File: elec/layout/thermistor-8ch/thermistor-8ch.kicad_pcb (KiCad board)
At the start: 4 copper layers, 29.7 x 28.3 mm, 78 parts, among them U5 10µH ±20%

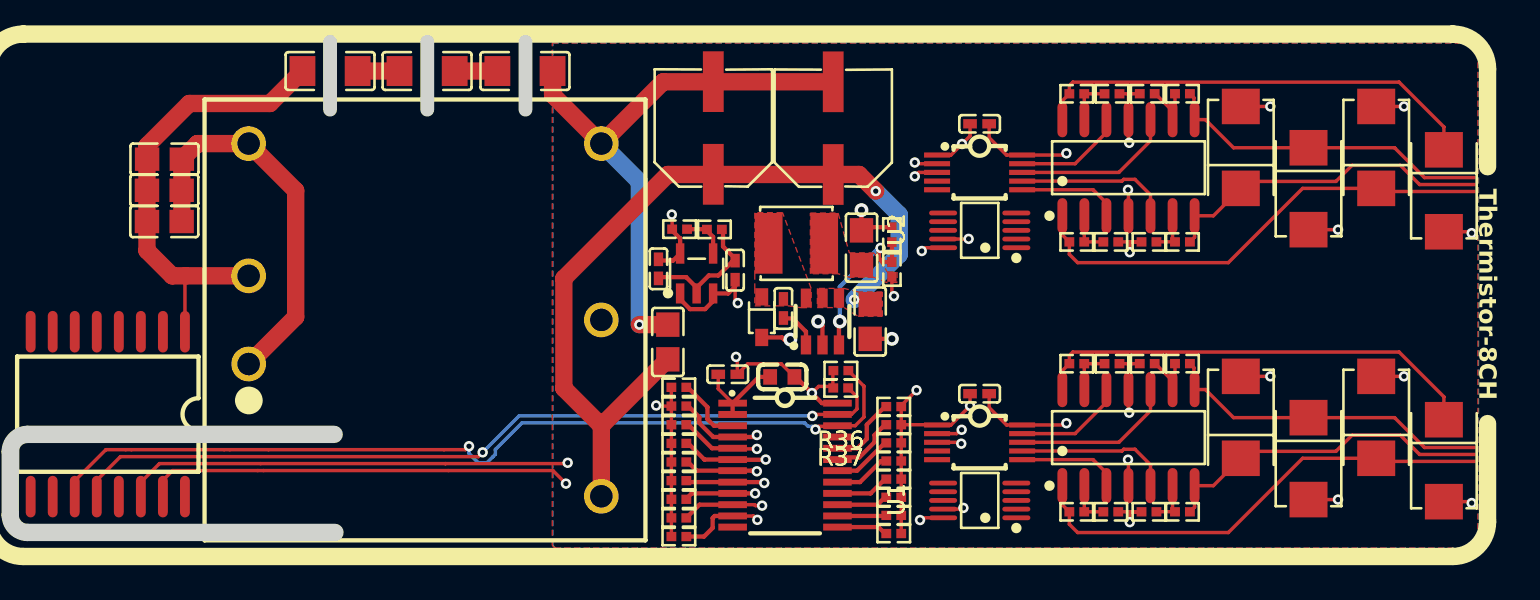
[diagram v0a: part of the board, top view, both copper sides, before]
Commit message: connect up ADC to thermistor outputs
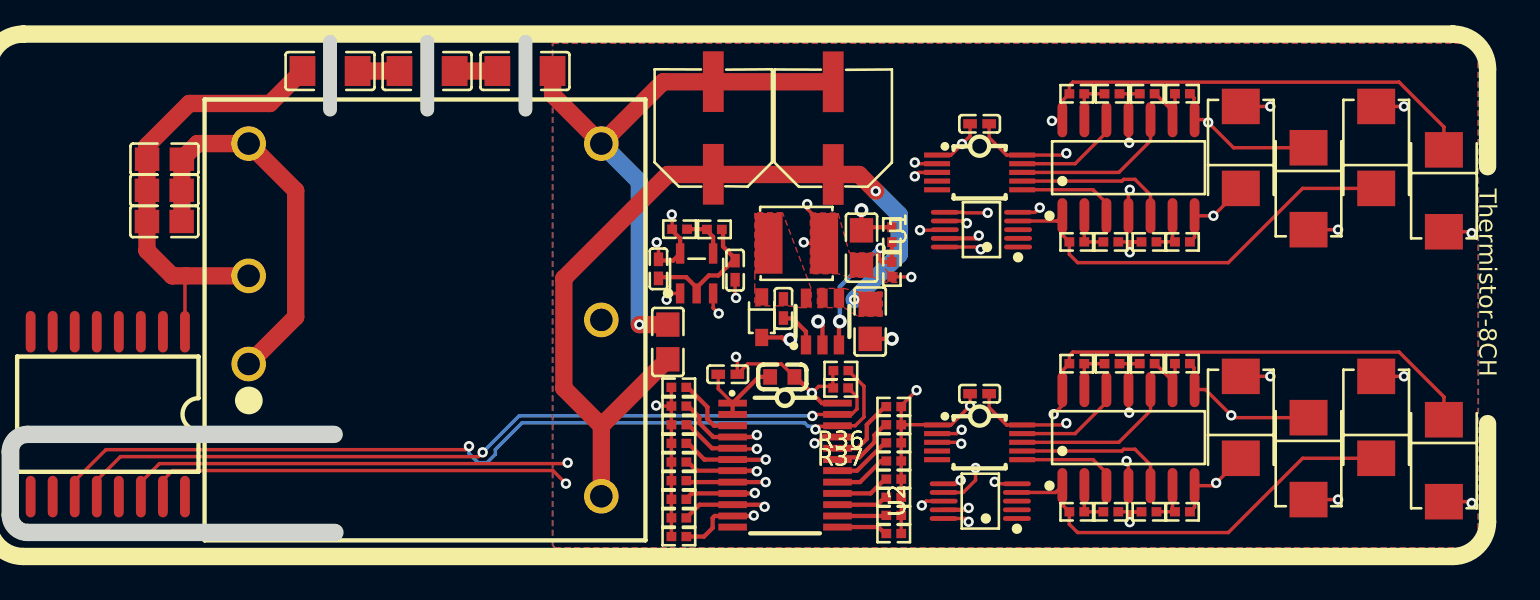
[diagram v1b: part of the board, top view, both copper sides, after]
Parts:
- moved U1 15.6 mm to (109.6, 88.7)
- moved U2 15.6 mm to (109.6, 104.3)
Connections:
- net SW renamed cathode
- net dac_1_4-IN3plus renamed IN3plus
- net dac_1_4-VOUTD renamed dac_1_4-IN4plus
- net dac_5_8-IN3plus renamed VOUTC
- net dac_5_8-VOUTD renamed dac_5_8-IN4plus
- C10 pad 1: hv-2 -> hv
- C10 pad 2: gnd -> gnd-1
- C11 pad 1: hv-2 -> hv
- C11 pad 2: gnd -> gnd-1
- C12 pad 1: hv-2 -> hv
- C12 pad 2: gnd -> gnd-1
- C13 pad 2: gnd-1 -> gnd
- C14 pad 2: gnd-1 -> gnd
- C15 pad 2: gnd-1 -> gnd
- C16 pad 1: gnd -> gnd-1
- C16 pad 2: regulator_24v_isolated-net -> regulator_24v_isolated-net-1
- C17 pad 1: regulator_24v_isolated-net -> regulator_24v_isolated-net-1
- C17 pad 2: regulator_24v_isolated-net-1 -> regulator_24v_isolated-net
- C18 pad 1: regulator_24v_isolated-net-1 -> regulator_24v_isolated-net
- C18 pad 2: gnd-1 -> gnd
- C2 pad 2: gnd-1 -> gnd
- C3 pad 1: hv -> hv-2
- C3 pad 2: gnd-1 -> gnd
- C4 pad 2: gnd-1 -> gnd
- C5 pad 2: gnd-1 -> gnd
- C6 pad 2: gnd-1 -> gnd
- C7 pad 2: gnd-1 -> gnd
- C8 pad 1: hv -> hv-2
- C8 pad 2: gnd-1 -> gnd
- C9 pad 2: gnd-1 -> gnd
- D1 pad 1: line-4 -> line-13
- D1 pad 2: gnd-1 -> gnd
- D2 pad 1: line-19 -> line-4
- D2 pad 2: gnd-1 -> gnd
- D3 pad 1: line-5 -> line-2
- D3 pad 2: gnd-1 -> gnd
- D4 pad 1: line-15 -> line-7
- D4 pad 2: gnd-1 -> gnd
- D5 pad 1: line-11 -> line-18
- D5 pad 2: gnd-1 -> gnd
- D6 pad 1: line-8 -> line-3
- D6 pad 2: gnd-1 -> gnd
- D7 pad 1: line-3 -> line-11
- D7 pad 2: gnd-1 -> gnd
- D8 pad 1: line-13 -> line
- D8 pad 2: gnd-1 -> gnd
- R1 pad 2: gnd-1 -> gnd
- R10 pad 1: gnd-1 -> gnd
- R11 pad 2: line-11 -> line-18
- R12 pad 1: gnd-1 -> gnd
- R13 pad 2: line-8 -> line-3
- R14 pad 1: gnd-1 -> gnd
- R15 pad 2: line-3 -> line-11
- R16 pad 1: gnd-1 -> gnd
- R17 pad 2: line-13 -> line
- R18 pad 1: gnd-1 -> gnd
- R19 pad 1: line-10 -> line-12
- R2 pad 1: hv -> hv-2
- R20 pad 1: line-18 -> line-10
- R21 pad 1: line-1 -> line-5
- R22 pad 1: line-12 -> line-16
- R23 pad 1: line-9 -> line-6
- R24 pad 1: line -> line-14
- R25 pad 1: line-7 -> line-8
- R26 pad 1: line-14 -> line-19
- R3 pad 2: line-4 -> line-13
- R36 pad 1: line-2 -> line-17
- R37 pad 1: line-6 -> line-9
- R38 pad 2: gnd-1 -> gnd
- R4 pad 1: gnd-1 -> gnd
- R5 pad 2: line-19 -> line-4
- R6 pad 1: gnd-1 -> gnd
- R7 pad 2: line-5 -> line-2
- R8 pad 1: gnd-1 -> gnd
- R9 pad 2: line-15 -> line-7
- U1 pad 1: gnd-1 -> gnd
- U1 pad 10: line-9 -> line-8
- U1 pad 2: adc_1_4-line-3 -> adc_1_4-line
- U1 pad 3: gnd-1 -> gnd
- U1 pad 4: adc_1_4-line-4 -> line-13
- U1 pad 5: adc_1_4-line-2 -> line-4
- U1 pad 6: adc_1_4-line -> line-2
- U1 pad 7: adc_1_4-line-1 -> line-7
- U1 pad 8: hv-4 -> hv-2
- U1 pad 9: line -> line-19
- U10 pad 1: gnd -> gnd-1
- U10 pad 11: line-2 -> line-17
- U10 pad 12: line-6 -> line-9
- U10 pad 15: gnd-1 -> gnd
- U10 pad 5: line-16 -> line-1
- U10 pad 6: line-17 -> line-15
- U11 pad 1: gnd-1 -> gnd
- U11 pad 10: line-14 -> line-19
- U11 pad 11: line-7 -> line-8
- U11 pad 12: gnd-1 -> gnd
- U11 pad 2: gnd-1 -> gnd
- U11 pad 21: gnd-1 -> gnd
- U11 pad 22: line-2 -> line-17
- U11 pad 23: line-6 -> line-9
- U11 pad 4: line-18 -> line-10
- U11 pad 5: line-10 -> line-12
- U11 pad 6: line-12 -> line-16
- U11 pad 7: line-1 -> line-5
- U11 pad 8: line -> line-14
- U11 pad 9: line-9 -> line-6
- U12 pad 1: hv -> hv-2
- U12 pad 2: gnd-1 -> gnd
- U12 pad 3: hv -> hv-2
- U13 pad 1: hv-2 -> hv
- U13 pad 2: gnd -> gnd-1
- U13 pad 3: hv-2 -> hv
- U13 pad 4: gnd-1 -> gnd
- U2 pad 1: gnd-1 -> gnd
- U2 pad 10: line-7 -> line-6
- U2 pad 2: adc_5_8-line-3 -> adc_5_8-line
- U2 pad 3: gnd-1 -> gnd
- U2 pad 4: adc_5_8-line -> line-18
- U2 pad 5: adc_5_8-line-1 -> line-3
- U2 pad 6: adc_5_8-line-4 -> line-11
- U2 pad 7: adc_5_8-line-2 -> line
- U2 pad 8: hv-4 -> hv-2
- U3 pad 2: gnd-1 -> gnd
- U4 pad 2: gnd-1 -> gnd
- U5 pad 2: hv -> hv-2
- U6 pad 1: line-4 -> line-13
- U6 pad 11: gnd-1 -> gnd
- U6 pad 14: line-15 -> line-7
- U6 pad 4: hv -> hv-2
- U6 pad 5: VOUTB -> IN2plus
- U6 pad 7: line-19 -> line-4
- U6 pad 8: line-5 -> line-2
- U7 pad 10: gnd-1 -> gnd
- U7 pad 2: line-10 -> line-12
- U7 pad 3: line-18 -> line-10
- U7 pad 7: VOUTB -> IN2plus
- U8 pad 1: line-11 -> line-18
- U8 pad 11: gnd-1 -> gnd
- U8 pad 14: line-13 -> line
- U8 pad 4: hv -> hv-2
- U8 pad 5: IN2plus -> VOUTB
- U8 pad 7: line-8 -> line-3
- U8 pad 8: line-3 -> line-11
- U9 pad 10: gnd-1 -> gnd
- U9 pad 2: line-1 -> line-5
- U9 pad 3: line-12 -> line-16
- U9 pad 7: IN2plus -> VOUTB
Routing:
- net gnd: track 26.5 -> 120.2 mm, vias 0 -> 21
- net gnd-1: track 119.6 -> 26.5 mm, vias 20 -> 0
- net line-17: track 0.00 -> 52.5 mm, vias 0 -> 2
- net line-9: track 15.7 -> 47.9 mm
- net line-6: track 47.9 -> 18.6 mm
- net line-15: track 26.7 -> 0.00 mm
- net line-2: track 52.5 -> 26.6 mm
- net line-16: track 0.00 -> 20.9 mm, vias 0 -> 2
- net line: track 17.8 -> 37.7 mm
- net line-1: track 18.6 -> 0.00 mm, vias 2 -> 0
- net line-14: track 33.6 -> 18.4 mm
- net line-12: track 20.9 -> 34.6 mm
- net hv: track 10.6 -> 22.8 mm, vias 4 -> 0
- net line-4: track 28.3 -> 17.0 mm, vias 0 -> 2
- net line-8: track 19.9 -> 30.5 mm, vias 0 -> 2
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- added copper zone on B.Cu, net (none)
- added copper zone on F.Cu, net (none)
- added copper zone on F.Cu, net gnd
- added copper zone on In1.Cu, net gnd
- removed copper zone on F.Cu, net gnd-1
- removed copper zone on In1.Cu, net gnd-1
- removed copper zone on B.Cu, net hv
- removed copper zone on F.Cu, net hv

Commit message: building frozen
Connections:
- net IN2plus renamed dac_1_4-VOUTB
- net VOUTB renamed dac_5_8-VOUTB
- net cathode renamed SW
- net dac_1_4-IN4plus renamed dac_1_4-VOUTD
- net dac_5_8-IN4plus renamed dac_5_8-VOUTD
- C10 pad 1: hv -> hv-2
- C10 pad 2: gnd-1 -> gnd
- C11 pad 1: hv -> hv-2
- C11 pad 2: gnd-1 -> gnd
- C12 pad 1: hv -> hv-2
- C12 pad 2: gnd-1 -> gnd
- C13 pad 1: hv-1 -> hv-4
- C13 pad 2: gnd -> gnd-1
- C14 pad 1: hv-1 -> hv-4
- C14 pad 2: gnd -> gnd-1
- C15 pad 1: hv-1 -> hv-4
- C15 pad 2: gnd -> gnd-1
- C16 pad 1: gnd-1 -> gnd
- C18 pad 2: gnd -> gnd-1
- C2 pad 1: hv-1 -> hv-4
- C2 pad 2: gnd -> gnd-1
- C3 pad 1: hv-2 -> hv
- C3 pad 2: gnd -> gnd-1
- C4 pad 1: hv-4 -> hv-1
- C4 pad 2: gnd -> gnd-1
- C5 pad 1: hv-4 -> hv-1
- C5 pad 2: gnd -> gnd-1
- C6 pad 1: hv-4 -> hv-1
- C6 pad 2: gnd -> gnd-1
- C7 pad 1: hv-4 -> hv-1
- C7 pad 2: gnd -> gnd-1
- C8 pad 1: hv-2 -> hv
- C8 pad 2: gnd -> gnd-1
- C9 pad 1: hv-4 -> hv-1
- C9 pad 2: gnd -> gnd-1
- D1 pad 1: line-13 -> line-8
- D1 pad 2: gnd -> gnd-1
- D2 pad 1: line-4 -> line-12
- D2 pad 2: gnd -> gnd-1
- D3 pad 1: line-2 -> line-17
- D3 pad 2: gnd -> gnd-1
- D4 pad 1: line-7 -> line-14
- D4 pad 2: gnd -> gnd-1
- D5 pad 1: line-18 -> line-15
- D5 pad 2: gnd -> gnd-1
- D6 pad 1: line-3 -> line-7
- D6 pad 2: gnd -> gnd-1
- D7 pad 1: line-11 -> line-13
- D7 pad 2: gnd -> gnd-1
- D8 pad 1: line -> line-2
- D8 pad 2: gnd -> gnd-1
- R1 pad 2: gnd -> gnd-1
- R10 pad 1: gnd -> gnd-1
- R11 pad 2: line-18 -> line-15
- R12 pad 1: gnd -> gnd-1
- R13 pad 2: line-3 -> line-7
- R14 pad 1: gnd -> gnd-1
- R15 pad 2: line-11 -> line-13
- R16 pad 1: gnd -> gnd-1
- R17 pad 2: line -> line-2
- R18 pad 1: gnd -> gnd-1
- R19 pad 1: line-12 -> line-18
- R19 pad 2: hv-4 -> hv-1
- R2 pad 1: hv-2 -> hv
- R20 pad 1: line-10 -> line-4
- R20 pad 2: hv-4 -> hv-1
- R21 pad 1: line-5 -> line-6
- R21 pad 2: hv-4 -> hv-1
- R22 pad 1: line-16 -> line
- R22 pad 2: hv-4 -> hv-1
- R23 pad 1: line-6 -> line-1
- R23 pad 2: hv-4 -> hv-1
- R24 pad 1: line-14 -> line-16
- R24 pad 2: hv-4 -> hv-1
- R25 pad 1: line-8 -> line-3
- R25 pad 2: hv-4 -> hv-1
- R26 pad 1: line-19 -> line-10
- R26 pad 2: hv-4 -> hv-1
- R27 pad 2: hv-4 -> hv-1
- R28 pad 2: hv-4 -> hv-1
- R29 pad 2: hv-4 -> hv-1
- R3 pad 2: line-13 -> line-8
- R30 pad 2: hv-4 -> hv-1
- R31 pad 2: hv-4 -> hv-1
- R32 pad 2: hv-4 -> hv-1
- R33 pad 2: hv-4 -> hv-1
- R34 pad 2: hv-4 -> hv-1
- R35 pad 2: hv-4 -> hv-1
- R36 pad 1: line-17 -> line-5
- R36 pad 2: hv-4 -> hv-1
- R37 pad 2: hv-4 -> hv-1
- R38 pad 2: gnd -> gnd-1
- R39 pad 1: hv-4 -> hv-1
- R4 pad 1: gnd -> gnd-1
- R5 pad 2: line-4 -> line-12
- R6 pad 1: gnd -> gnd-1
- R7 pad 2: line-2 -> line-17
- R8 pad 1: gnd -> gnd-1
- R9 pad 2: line-7 -> line-14
- U1 pad 1: gnd -> gnd-1
- U1 pad 10: line-8 -> line-3
- U1 pad 3: gnd -> gnd-1
- U1 pad 4: line-13 -> line-8
- U1 pad 5: line-4 -> line-12
- U1 pad 6: line-2 -> line-17
- U1 pad 7: line-7 -> line-14
- U1 pad 8: hv-2 -> hv
- U1 pad 9: line-19 -> line-10
- U10 pad 1: gnd-1 -> gnd
- U10 pad 11: line-17 -> line-5
- U10 pad 14: hv-4 -> hv-1
- U10 pad 15: gnd -> gnd-1
- U10 pad 5: line-1 -> line-11
- U10 pad 6: line-15 -> line-19
- U11 pad 1: gnd -> gnd-1
- U11 pad 10: line-19 -> line-10
- U11 pad 11: line-8 -> line-3
- U11 pad 12: gnd -> gnd-1
- U11 pad 2: gnd -> gnd-1
- U11 pad 21: gnd -> gnd-1
- U11 pad 22: line-17 -> line-5
- U11 pad 24: hv-4 -> hv-1
- U11 pad 4: line-10 -> line-4
- U11 pad 5: line-12 -> line-18
- U11 pad 6: line-16 -> line
- U11 pad 7: line-5 -> line-6
- U11 pad 8: line-14 -> line-16
- U11 pad 9: line-6 -> line-1
- U12 pad 1: hv-2 -> hv
- U12 pad 2: gnd -> gnd-1
- U12 pad 3: hv-2 -> hv
- U12 pad 5: hv-4 -> hv-1
- U13 pad 1: hv -> hv-2
- U13 pad 2: gnd-1 -> gnd
- U13 pad 3: hv -> hv-2
- U13 pad 4: gnd -> gnd-1
- U13 pad 6: hv-1 -> hv-4
- U2 pad 1: gnd -> gnd-1
- U2 pad 10: line-6 -> line-1
- U2 pad 3: gnd -> gnd-1
- U2 pad 4: line-18 -> line-15
- U2 pad 5: line-3 -> line-7
- U2 pad 6: line-11 -> line-13
- U2 pad 7: line -> line-2
- U2 pad 8: hv-2 -> hv
- U2 pad 9: line-14 -> line-16
- U3 pad 2: gnd -> gnd-1
- U4 pad 2: gnd -> gnd-1
- U4 pad 4: hv-1 -> hv-4
- U4 pad 5: hv-1 -> hv-4
- U5 pad 2: hv-2 -> hv
- U6 pad 1: line-13 -> line-8
- U6 pad 10: IN3plus -> VOUTC
- U6 pad 11: gnd -> gnd-1
- U6 pad 14: line-7 -> line-14
- U6 pad 4: hv-2 -> hv
- U6 pad 7: line-4 -> line-12
- U6 pad 8: line-2 -> line-17
- U7 pad 1: hv-4 -> hv-1
- U7 pad 10: gnd -> gnd-1
- U7 pad 2: line-12 -> line-18
- U7 pad 3: line-10 -> line-4
- U7 pad 8: IN3plus -> VOUTC
- U8 pad 1: line-18 -> line-15
- U8 pad 10: VOUTC -> IN3plus
- U8 pad 11: gnd -> gnd-1
- U8 pad 14: line -> line-2
- U8 pad 4: hv-2 -> hv
- U8 pad 7: line-3 -> line-7
- U8 pad 8: line-11 -> line-13
- U9 pad 1: hv-4 -> hv-1
- U9 pad 10: gnd -> gnd-1
- U9 pad 2: line-5 -> line-6
- U9 pad 3: line-16 -> line
- U9 pad 8: VOUTC -> IN3plus
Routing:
- net gnd-1: track 26.5 -> 120.2 mm, vias 0 -> 21
- net gnd: track 120.2 -> 26.5 mm, vias 21 -> 0
- net line-5: track 18.6 -> 52.5 mm
- net line-19: track 30.1 -> 0.00 mm, vias 2 -> 0
- net line-11: track 27.2 -> 0.00 mm, vias 2 -> 0
- net line-17: track 52.5 -> 26.6 mm
- net line-15: track 0.00 -> 25.3 mm
- net hv-4: track 67.4 -> 47.6 mm, vias 9 -> 2
- net hv-1: track 47.6 -> 67.4 mm, vias 2 -> 9
- net line-1: track 0.00 -> 18.6 mm, vias 0 -> 2
- net line-14: track 18.4 -> 36.1 mm
- net line-12: track 34.6 -> 17.0 mm
- net line-4: track 17.0 -> 34.2 mm
- net line: track 37.7 -> 20.9 mm
- net line-7: track 36.1 -> 19.5 mm
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- added copper zone on F.Cu, net gnd-1
- added copper zone on In1.Cu, net gnd-1
- added copper zone on In2.Cu, net hv-1
- added copper zone on F.Cu, net hv-4
- removed copper zone on F.Cu, net gnd
- removed copper zone on In1.Cu, net gnd
- removed copper zone on F.Cu, net hv-1
- removed copper zone on In2.Cu, net hv-4
